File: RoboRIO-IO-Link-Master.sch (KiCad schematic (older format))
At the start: 22 parts, among them J1 IO-Link-Jack, J2 IO-Link-Jack, J3 IO-Link-Jack, J4 IO-Link-Jack, J5 Board Power, J6 RoboRIO-SPI, U1 TPS61175PWP

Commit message: New step up that can handle 2A (instead of only 400mA)
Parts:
- removed C1: 4.7uF-3.705m, symbol Device:C
- removed C5: 10uF-40m, symbol Device:CP1
- removed C6, C7: 1uF-1m, symbol Device:C
- removed D1: 650mV-3A, symbol Device:D_Schottky_ALT
- removed U1: TPS61175PWP, PWP14_2P31X2P46, symbol TPS61175PWP:TPS61175PWP
- added 1: CSD17304Q3, DQG0008A, symbol CSD17304Q3:CSD17304Q3
- added C1: 100uF-160m, symbol Device:CP1
- added C5: 10pF, symbol Device:C
- added C? (x2): 82uF-20m, symbol Device:CP1
- added D1: 950mV-10A, symbol Device:D_Schottky
- added R62: 100, symbol Device:R_US
- added R63: 6m, symbol Device:R_US
- added U1: LM3488MMX_NOPB, MUA08A, symbol LM3488MMX-NOPB:LM3488MMX_NOPB
- C2: value 4.7uF-3.705m -> 100nF-1m
- C3: value 47nF -> 1nF
- C4: value 10nF -> 22nF
- L1: value 12uH-70mOhm -> 4.7uH-13m
- R1: value 86.6k -> 4.42k
- R2: value 6.98k -> 1k
- R3: value 300k -> 18.2k
- R4: value 16.2k -> 26.1k
- gave numbers to parts that had none: 1
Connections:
- wire segments 151 -> 144
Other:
- note added: "IO-Link Device Jacks&Masters"
- note added: "RoboRIO SPI Jack\n"
- note removed: "IO-Link Device Jacks"
- moved on the sheet: J1, J2, J3, J4, J5, J6, R18, Y1

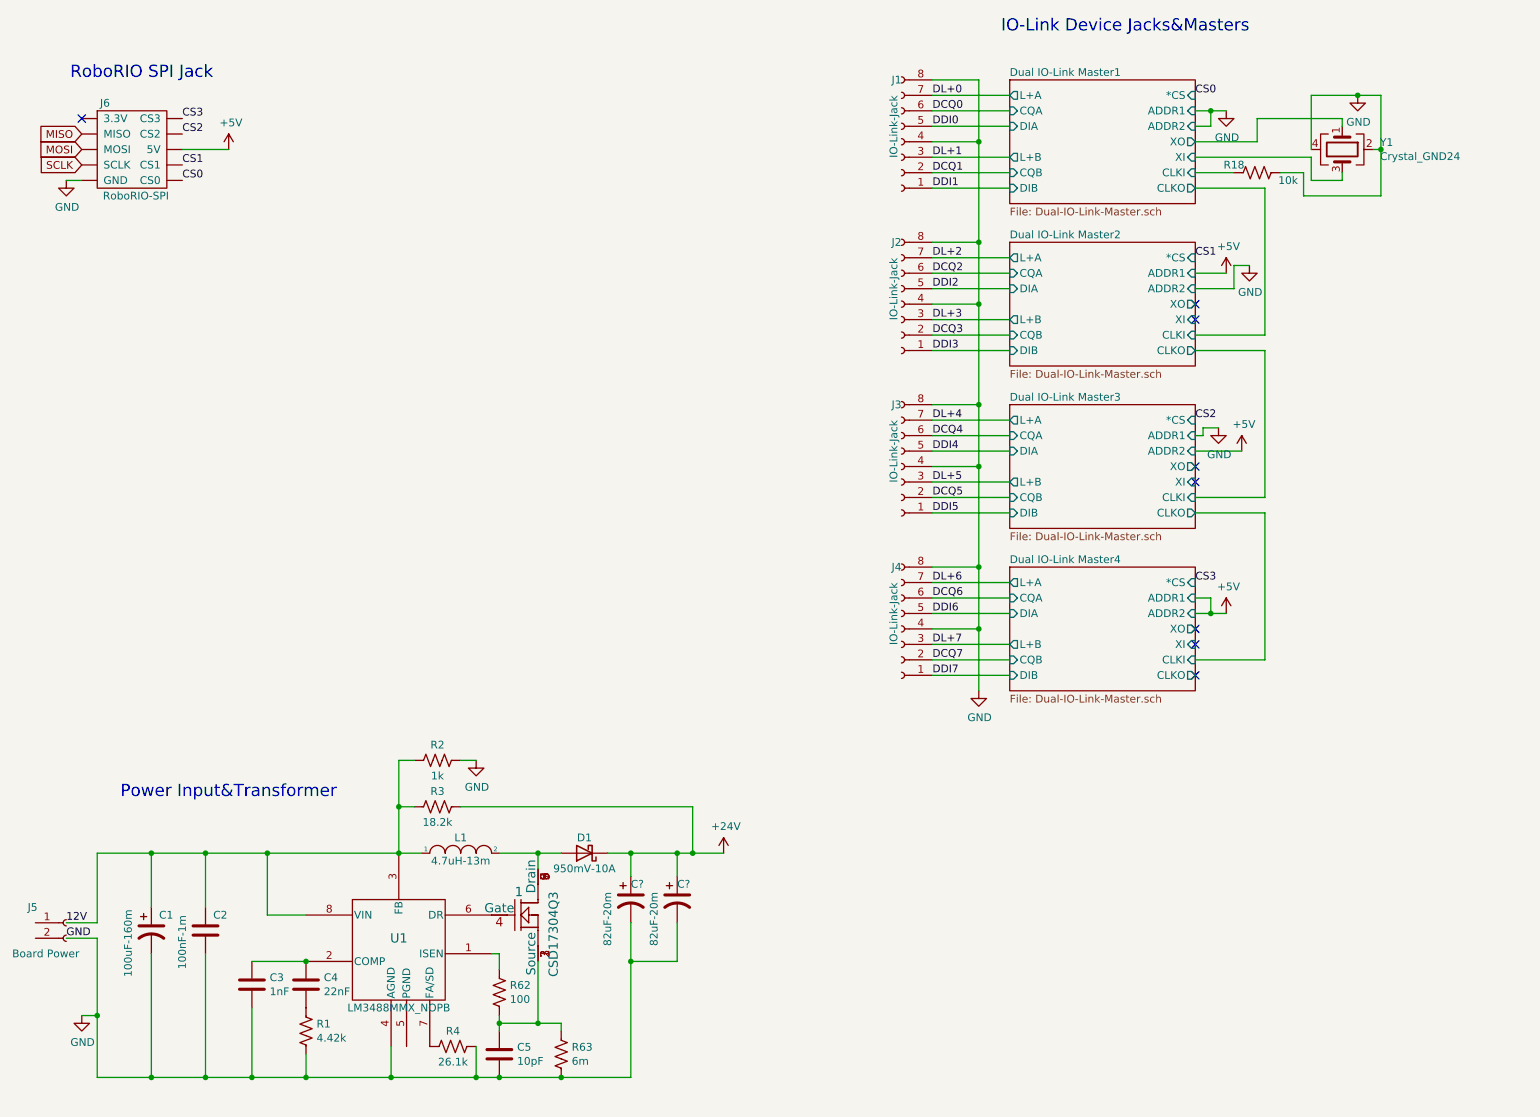
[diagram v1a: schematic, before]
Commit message: Wrapping up schematics for the MAX14819s
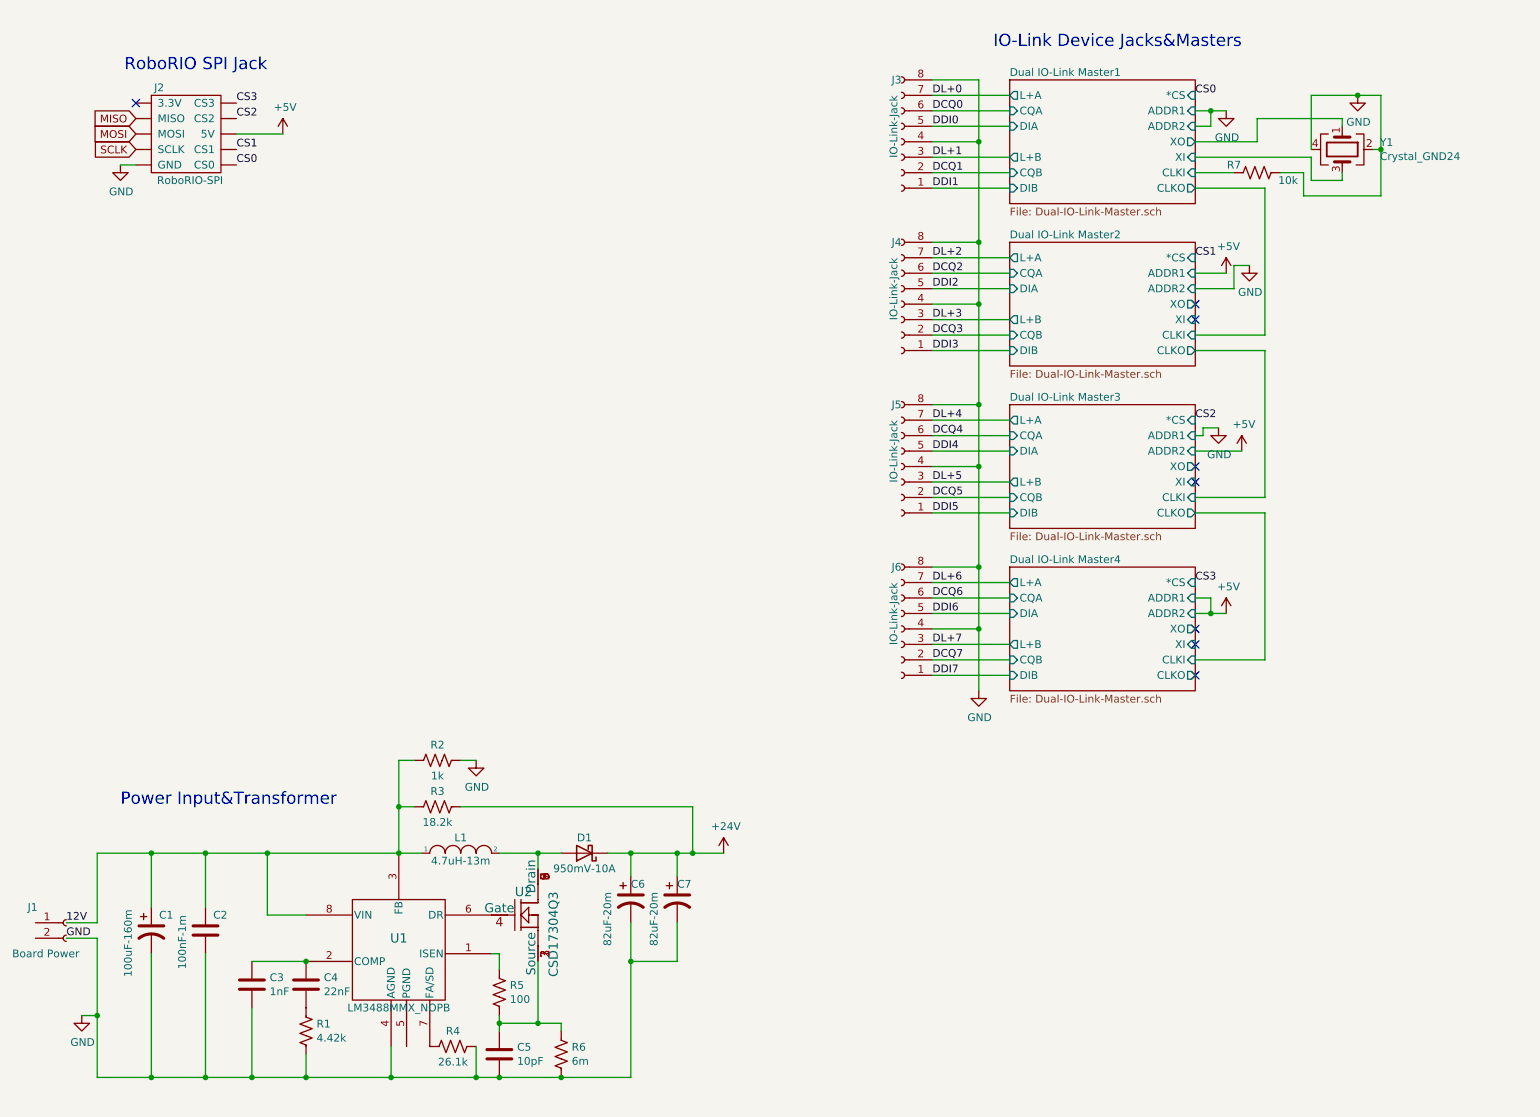
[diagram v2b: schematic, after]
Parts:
- gave numbers to parts that had none: 2
- renumbered J5 to J1, J6 to J2, J1 to J3, J2 to J4, J3 to J5, J4 to J6, R62 to R5, R63 to R6, R18 to R7, 1 to U2
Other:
- moved on the sheet: J2
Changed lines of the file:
@@
 $EndDescr
 $Comp
-L CustomSymbols:RoboRIO-SPI J6
+L CustomSymbols:RoboRIO-SPI J2
 U 1 1 60718BD4
-P 1450 1600
-F 0 "J6" H 1250 1950 50  0000 C CNN
-F 1 "RoboRIO-SPI" H 1450 1350 50  0000 C CNN
-F 2 "" H 2100 1600 50  0001 C CNN
-F 3 "" H 2100 1600 50  0001 C CNN
-	1    1450 1600
-	1    0    0    -1
-$EndComp
-$Comp
-L Connector:Conn_01x02_Female J5
+P 1800 1500
+F 0 "J2" H 1600 1850 50  0000 C CNN
+F 1 "RoboRIO-SPI" H 1800 1250 50  0000 C CNN
+F 2 "" H 2450 1500 50  0001 C CNN
+F 3 "" H 2450 1500 50  0001 C CNN
+	1    1800 1500
+	1    0    0    -1
+$EndComp
+$Comp
+L Connector:Conn_01x02_Female J1
 U 1 1 607234CA
 P 1000 6550
-F 0 "J5" H 750 6650 50  0000 L CNN
+F 0 "J1" H 750 6650 50  0000 L CNN
 F 1 "Board Power" H 650 6350 50  0000 L CNN
 F 2 "" H 1000 6550 50  0001 C CNN
@@
 $EndComp
 $Comp
-L Connector:Conn_01x08_Female J1
+L Connector:Conn_01x08_Female J3
 U 1 1 6073B5D7
 P 6400 1500
-F 0 "J1" H 6400 1100 50  0000 L CNN
+F 0 "J3" H 6400 1100 50  0000 L CNN
 F 1 "IO-Link-Jack" V 6450 1200 50  0000 L CNN
 F 2 "" H 6400 1500 50  0001 C CNN
@@
 $EndComp
 $Comp
-L power:GND #PWR01
+L power:GND #PWR02
 U 1 1 6074491F
-P 1000 1750
-F 0 "#PWR01" H 1000 1500 50  0001 C CNN
-F 1 "GND" H 1005 1577 50  0000 C CNN
-F 2 "" H 1000 1750 50  0001 C CNN
-F 3 "" H 1000 1750 50  0001 C CNN
-	1    1000 1750
-	1    0    0    -1
-$EndComp
-Wire Wire Line
-	1000 1750 1100 1750
+P 1350 1650
+F 0 "#PWR02" H 1350 1400 50  0001 C CNN
+F 1 "GND" H 1355 1477 50  0000 C CNN
+F 2 "" H 1350 1650 50  0001 C CNN
+F 3 "" H 1350 1650 50  0001 C CNN
+	1    1350 1650
+	1    0    0    -1
+$EndComp
+Wire Wire Line
+	1350 1650 1450 1650
 $Comp
 L power:+24V #PWR05
@@
 	1    0    0    -1
 $EndComp
-Text Label 1750 1350 0    50   ~ 0
+Text Label 2100 1250 0    50   ~ 0
 CS3
-Text Label 1750 1450 0    50   ~ 0
+Text Label 2100 1350 0    50   ~ 0
 CS2
-Text Label 1750 1650 0    50   ~ 0
+Text Label 2100 1550 0    50   ~ 0
 CS1
-Text Label 1750 1750 0    50   ~ 0
+Text Label 2100 1650 0    50   ~ 0
 CS0
-NoConn ~ 1100 1350
+NoConn ~ 1450 1250
 $Comp
 L power:+5V #PWR03
 U 1 1 6074D982
-P 2050 1550
-F 0 "#PWR03" H 2050 1400 50  0001 C CNN
-F 1 "+5V" H 2065 1723 50  0000 C CNN
-F 2 "" H 2050 1550 50  0001 C CNN
-F 3 "" H 2050 1550 50  0001 C CNN
-	1    2050 1550
-	1    0    0    -1
-$EndComp
-Wire Wire Line
-	1750 1550 2050 1550
+P 2400 1450
+F 0 "#PWR03" H 2400 1300 50  0001 C CNN
+F 1 "+5V" H 2415 1623 50  0000 C CNN
+F 2 "" H 2400 1450 50  0001 C CNN
+F 3 "" H 2400 1450 50  0001 C CNN
+	1    2400 1450
+	1    0    0    -1
+$EndComp
+Wire Wire Line
+	2100 1450 2400 1450
 Text Label 1000 6550 0    50   ~ 0
 12V
@@
 GND
 $Comp
-L Connector:Conn_01x08_Female J2
+L Connector:Conn_01x08_Female J4
 U 1 1 607CEB78
 P 6400 2550
-F 0 "J2" H 6400 2150 50  0000 L CNN
+F 0 "J4" H 6400 2150 50  0000 L CNN
 F 1 "IO-Link-Jack" V 6450 2250 50  0000 L CNN
 F 2 "" H 6400 2550 50  0001 C CNN
@@
 $EndComp
 $Comp
-L Connector:Conn_01x08_Female J3
+L Connector:Conn_01x08_Female J5
 U 1 1 607CFD14
 P 6400 3600
-F 0 "J3" H 6400 3200 50  0000 L CNN
+F 0 "J5" H 6400 3200 50  0000 L CNN
 F 1 "IO-Link-Jack" V 6450 3300 50  0000 L CNN
 F 2 "" H 6400 3600 50  0001 C CNN
@@
 $EndComp
 $Comp
-L Connector:Conn_01x08_Female J4
+L Connector:Conn_01x08_Female J6
 U 1 1 607D08D5
 P 6400 4650
-F 0 "J4" H 6400 4250 50  0000 L CNN
+F 0 "J6" H 6400 4250 50  0000 L CNN
 F 1 "IO-Link-Jack" V 6450 4350 50  0000 L CNN
 F 2 "" H 6400 4650 50  0001 C CNN
@@
 $EndComp
 $Comp
-L power:GND #PWR02
+L power:GND #PWR06
 U 1 1 607D8265
 P 6900 5050
-F 0 "#PWR02" H 6900 4800 50  0001 C CNN
+F 0 "#PWR06" H 6900 4800 50  0001 C CNN
 F 1 "GND" H 6905 4877 50  0000 C CNN
 F 2 "" H 6900 5050 50  0001 C CNN
@@
 Text Label 6600 4750 0    50   ~ 0
 DL+7
-Text Notes 1350 5750 0    79   ~ 0
+Text Notes 1350 5800 0    79   ~ 0
 Power Input&Transformer\n
-Text Notes 8650 800  2    79   ~ 0
+Text Notes 8600 900  2    79   ~ 0
 IO-Link Device Jacks&Masters
-Text GLabel 1100 1450 0    50   Input ~ 0
+Text GLabel 1450 1350 0    50   Input ~ 0
 MISO
-Text GLabel 1100 1550 0    50   Input ~ 0
+Text GLabel 1450 1450 0    50   Input ~ 0
 MOSI
-Text GLabel 1100 1650 0    50   Input ~ 0
+Text GLabel 1450 1550 0    50   Input ~ 0
 SCLK
 $Sheet
@@
 CS3
 $Comp
-L power:GND #PWR019
+L power:GND #PWR08
 U 1 1 60BD0847
 P 8500 1300
-F 0 "#PWR019" H 8500 1050 50  0001 C CNN
+F 0 "#PWR08" H 8500 1050 50  0001 C CNN
 F 1 "GND" H 8505 1127 50  0000 C CNN
 F 2 "" H 8500 1300 50  0001 C CNN
@@
 Connection ~ 8400 4550
 $Comp
-L power:+5V #PWR021
+L power:+5V #PWR010
 U 1 1 60BE19D9
 P 8500 4550
-F 0 "#PWR021" H 8500 4400 50  0001 C CNN
+F 0 "#PWR010" H 8500 4400 50  0001 C CNN
 F 1 "+5V" H 8515 4723 50  0000 C CNN
 F 2 "" H 8500 4550 50  0001 C CNN
@@
 	8300 3400 8350 3400
 $Comp
-L power:+5V #PWR022
+L power:+5V #PWR011
 U 1 1 60BF130A
 P 8600 3500
-F 0 "#PWR022" H 8600 3350 50  0001 C CNN
+F 0 "#PWR011" H 8600 3350 50  0001 C CNN
 F 1 "+5V" H 8615 3673 50  0000 C CNN
 F 2 "" H 8600 3500 50  0001 C CNN
@@
 	8300 3500 8600 3500
 $Comp
-L power:GND #PWR018
+L power:GND #PWR07
 U 1 1 60BFBB7A
 P 8450 3350
-F 0 "#PWR018" H 8450 3100 50  0001 C CNN
+F 0 "#PWR07" H 8450 3100 50  0001 C CNN
 F 1 "GND" H 8455 3177 50  0000 C CNN
 F 2 "" H 8450 3350 50  0001 C CNN
@@
 	8350 3350 8450 3350
 $Comp
-L power:GND #PWR023
+L power:GND #PWR012
 U 1 1 60BFCA45
 P 8650 2300
-F 0 "#PWR023" H 8650 2050 50  0001 C CNN
+F 0 "#PWR012" H 8650 2050 50  0001 C CNN
 F 1 "GND" H 8655 2127 50  0000 C CNN
 F 2 "" H 8650 2300 50  0001 C CNN
@@
 	8300 2350 8500 2350
 $Comp
-L power:+5V #PWR020
+L power:+5V #PWR09
 U 1 1 60BF6F2E
 P 8500 2350
-F 0 "#PWR020" H 8500 2200 50  0001 C CNN
+F 0 "#PWR09" H 8500 2200 50  0001 C CNN
 F 1 "+5V" H 8515 2523 50  0000 C CNN
 F 2 "" H 8500 2350 50  0001 C CNN
@@
 	8300 1700 8550 1700
 $Comp
-L Device:R_US R18
+L Device:R_US R7
 U 1 1 60CDFBCF
 P 8700 1700
-F 0 "R18" V 8650 1550 50  0000 C CNN
+F 0 "R7" V 8650 1550 50  0000 C CNN
 F 1 "10k" V 8750 1900 50  0000 C CNN
 F 2 "" V 8740 1690 50  0001 C CNN
@@
 	8850 1700 9000 1700
 $Comp
-L power:GND #PWR04
+L power:GND #PWR013
 U 1 1 60CED433
 P 9350 1200
-F 0 "#PWR04" H 9350 950 50  0001 C CNN
+F 0 "#PWR013" H 9350 950 50  0001 C CNN
 F 1 "GND" H 9355 1027 50  0000 C CNN
 F 2 "" H 9350 1200 50  0001 C CNN
@@
 	3150 6100 3300 6100
 $Comp
-L power:GND #PWR060
+L power:GND #PWR01
 U 1 1 60DA3A7F
 P 1100 7150
-F 0 "#PWR060" H 1100 6900 50  0001 C CNN
+F 0 "#PWR01" H 1100 6900 50  0001 C CNN
 F 1 "GND" H 1105 6977 50  0000 C CNN
 F 2 "" H 1100 7150 50  0001 C CNN
@@
 	3550 5500 3650 5500
 $Comp
-L power:GND #PWR061
+L power:GND #PWR04
 U 1 1 60DEF894
 P 3650 5500
-F 0 "#PWR061" H 3650 5250 50  0001 C CNN
+F 0 "#PWR04" H 3650 5250 50  0001 C CNN
 F 1 "GND" H 3655 5327 50  0000 C CNN
 F 2 "" H 3650 5500 50  0001 C CNN
@@
 $EndComp
 $Comp
-L CSD17304Q3:CSD17304Q3 1
+L CSD17304Q3:CSD17304Q3 U2
 U 1 1 60E02528
 P 3900 6500
-F 0 "1" H 3900 6650 60  0000 L CNN
+F 0 "U2" H 3900 6650 60  0000 L CNN
 F 1 "CSD17304Q3" V 4150 6100 60  0000 L CNN
 F 2 "DQG0008A" H 3900 6440 60  0001 C CNN
@@
 Connection ~ 3800 7550
 $Comp
-L Device:R_US R63
+L Device:R_US R6
 U 1 1 60E54CE8
 P 4200 7400
-F 0 "R63" H 4268 7446 50  0000 L CNN
+F 0 "R6" H 4268 7446 50  0000 L CNN
 F 1 "6m" H 4268 7355 50  0000 L CNN
 F 2 "" V 4240 7390 50  0001 C CNN
@@
 	4200 7200 4200 7250
 $Comp
-L Device:R_US R62
+L Device:R_US R5
 U 1 1 60E5FEBA
 P 3800 7000
-F 0 "R62" H 3868 7046 50  0000 L CNN
+F 0 "R5" H 3868 7046 50  0000 L CNN
 F 1 "100" H 3868 6955 50  0000 L CNN
 F 2 "" V 3840 6990 50  0001 C CNN
@@
 	4650 6100 4650 6250
 $Comp
-L Device:CP1 C?
+L Device:CP1 C6
 U 1 1 60E807DC
 P 4650 6400
-F 0 "C?" H 4650 6500 50  0000 L CNN
+F 0 "C6" H 4650 6500 50  0000 L CNN
 F 1 "82uF-20m" V 4500 6100 50  0000 L CNN
 F 2 "" H 4650 6400 50  0001 C CNN
@@
 $EndComp
 $Comp
-L Device:CP1 C?
+L Device:CP1 C7
 U 1 1 60E81E7F
 P 4950 6400
-F 0 "C?" H 4950 6500 50  0000 L CNN
+F 0 "C7" H 4950 6500 50  0000 L CNN
 F 1 "82uF-20m" V 4800 6100 50  0000 L CNN
 F 2 "" H 4950 6400 50  0001 C CNN
@@
 Wire Wire Line
 	5050 6100 5250 6100
-Text Notes 1950 1100 2    79   ~ 0
+Text Notes 2300 1050 2    79   ~ 0
 RoboRIO SPI Jack\n
 $EndSCHEMATC

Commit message: Schematic edits
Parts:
- removed U2: CSD17304Q3, DQG0008A, symbol CSD17304Q3:CSD17304Q3
- added C10, C11: 5pF, symbol Device:C
- added C3, C9: 10uF, symbol Device:C
- added D2: 3.3V, symbol Device:LED
- added D3: 10k, symbol Device:LED
- added D4: 22k, symbol Device:LED
- added D5: 46.7V, symbol Device:D_TVS
- added M1: CSD18504Q5A, TRANS_NexFET_Q5A, symbol CSD18504Q5A:CSD18504Q5A
- added R10: 10k, symbol Device:R_US
- added R11: 22k, symbol Device:R_US
- added R6: 0, symbol Device:R_US
- added R9: 1.5k, symbol Device:R_US
- added TP1: GND, symbol Connector:TestPoint
- added TP2: +12V, symbol Connector:TestPoint
- added TP3: +24V, symbol Connector:TestPoint
- added TVS1: SM30T47AY, CR_T12AY_STM, symbol SM30T47AY:SM30T12AY
- added TVS2: SM30T35AY, CR_T12AY_STM, symbol SM30T47AY:SM30T12AY
- added U1: SI4431BDY-T1-E3, SOIC-8_SI, symbol SI4431BDY-T1-E3:SI4431BDY-T1-E3
- J1: value Board Power -> Power In
- Y1: value Crystal_GND24 -> ABM3B-14.7456MHZ-10-1-U-T
- renumbered C3 to C4, C4 to C5, C5 to C6, C6 to C7, C7 to C8, R6 to R7, R7 to R8, U1 to U2
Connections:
- net +24V: now also C9.1, D4.2 (A), D5.1 (A1), TP3.1, TVS1.2 (K)
- net 12V: now also U1.5 (D), U1.6 (D), U1.7 (D), U1.8 (D); no longer C1.1, C2.1, L1.1, R2.2, R3.2, U2.3 (FB), U2.8 (VIN)
- net Dual IO-Link Master1/XI: now also C11.2
- net Dual IO-Link Master1/XO: now also C10.1
- net GND: now also R2.2, U2.5 (PGND), C10.2, C11.1, C3.2, C9.2, D5.2 (A2), R10.1, R11.1, R9.1, TP1.1, TVS2.2 (K), U1.4 (G); no longer R2.1
- net at U2.6 (DR): now also R6.2
- net at D1.2 (A), L1.2: now also M1.5 (Drain), M1.6 (Drain), M1.7 (Drain), M1.8 (Drain), M1.9 (Drain)
- net at C6.1, R5.2, R7.1: now also M1.1 (Source), M1.2 (Source), M1.3 (Source)
- new net: M1.4 (Gate), R6.1
- new net: D2.1 (K), R9.2
- new net: D3.1 (K), R10.2
- new net: D4.1 (K), R11.2
- new net: R2.1, R3.2, U2.3 (FB)
- new net +12V: C1.1, C2.1, C3.1, D3.2 (A), L1.1, TP2.1, U1.1 (S), U1.2 (S), U1.3 (S), U2.8 (VIN)
- new net +3V3: D2.2 (A), J2.~ (SCLK)
- new net TVS_CLAMP: TVS1.1 (A), TVS2.1 (A)
- no-connect marks 8 -> 7
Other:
- note added: "Power Input"
- note added: "Power Input & Boost\n\n"
- note added: "Power LEDs/Indicators\n"
- note added: "Transient Voltage Supression"
- note removed: "Power Input&Transformer\n"
- moved on the sheet: C1, C2, C4, C5, C6, C7, C8, D1, J1, J3, J4, J5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
